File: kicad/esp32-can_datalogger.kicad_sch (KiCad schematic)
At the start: 60 parts, among them J1 USB_C_Receptacle_USB2.0_16P, J2 USB_C_Receptacle_USB2.0_16P, J3 USB_C_Receptacle_USB2.0_16P, J4 USB_C_Receptacle_USB2.0_16P, J5 USB_C_Receptacle_USB2.0_16P, J6 USB_C_Receptacle_USB2.0_16P, J7 Conn_Coaxial, J8 MicroSD, J9 Conn_01x04_Socket, SW1 SW_Push, SW2 SW_Push, SW3 SW_Push, SW4 SW_Push, U2 PA1616D, U3 PI4ULS3V204LEX, U4 AZ1117-1.8, U5 TJA1051T, U6 TJA1051T, U7 ICM-20948

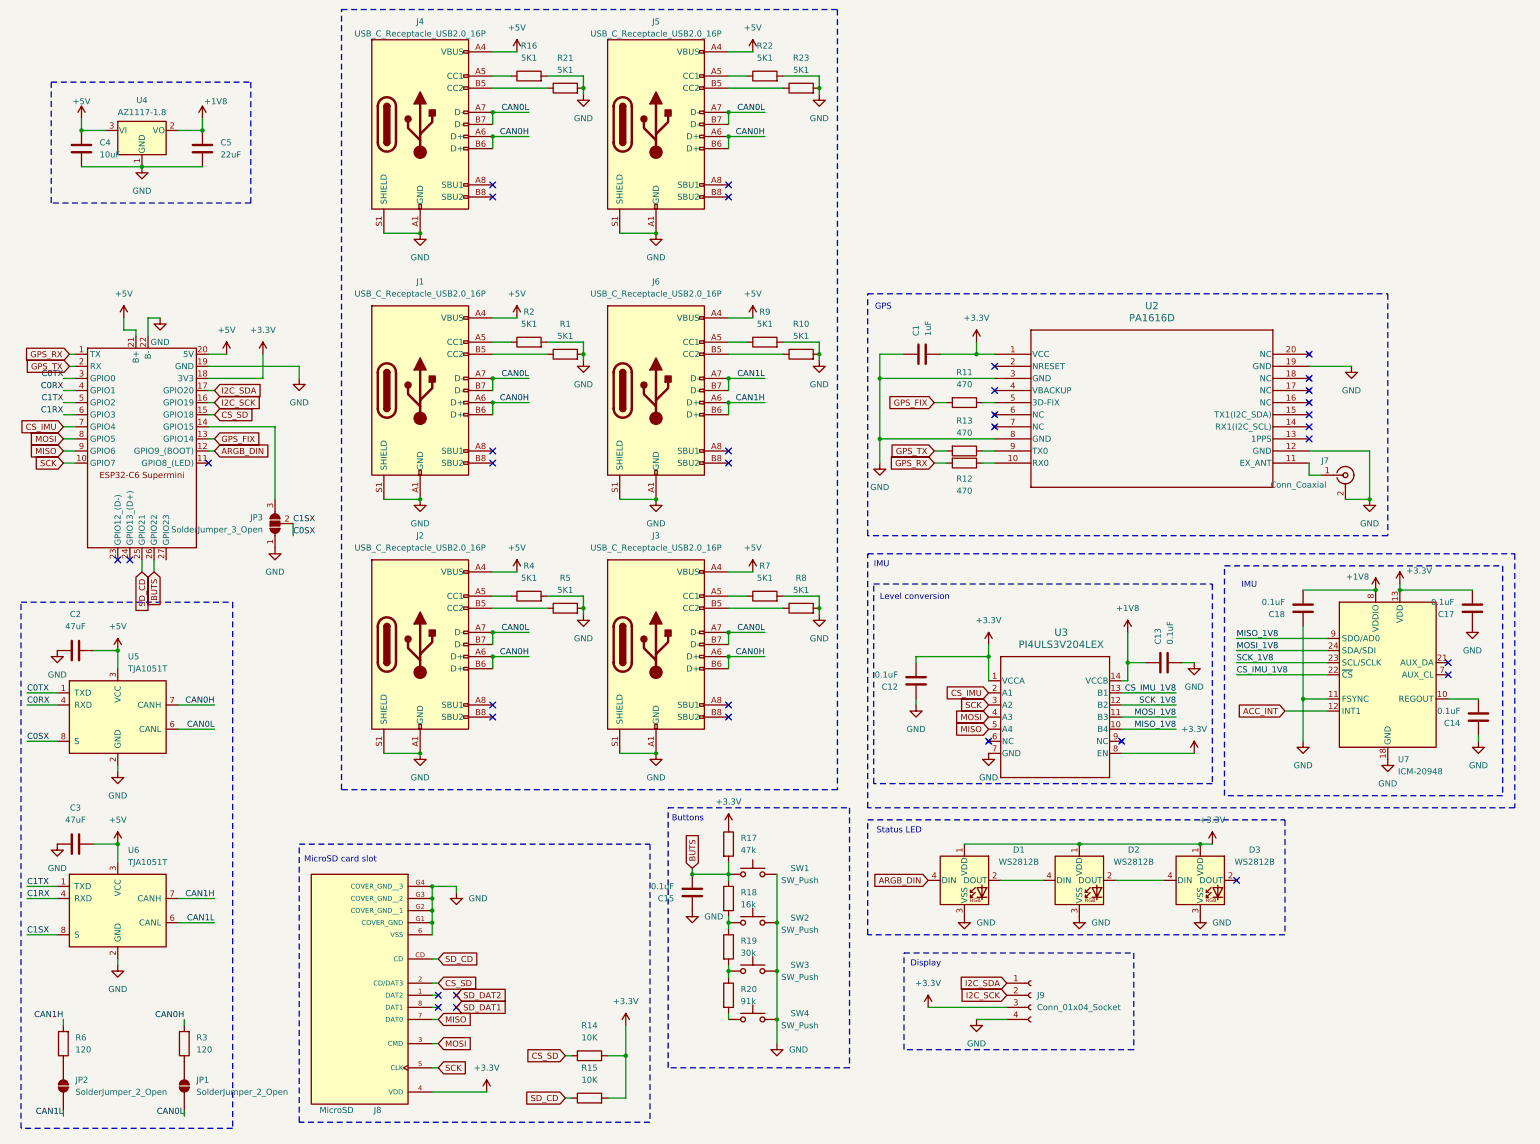
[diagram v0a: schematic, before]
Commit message: make pcb smaller
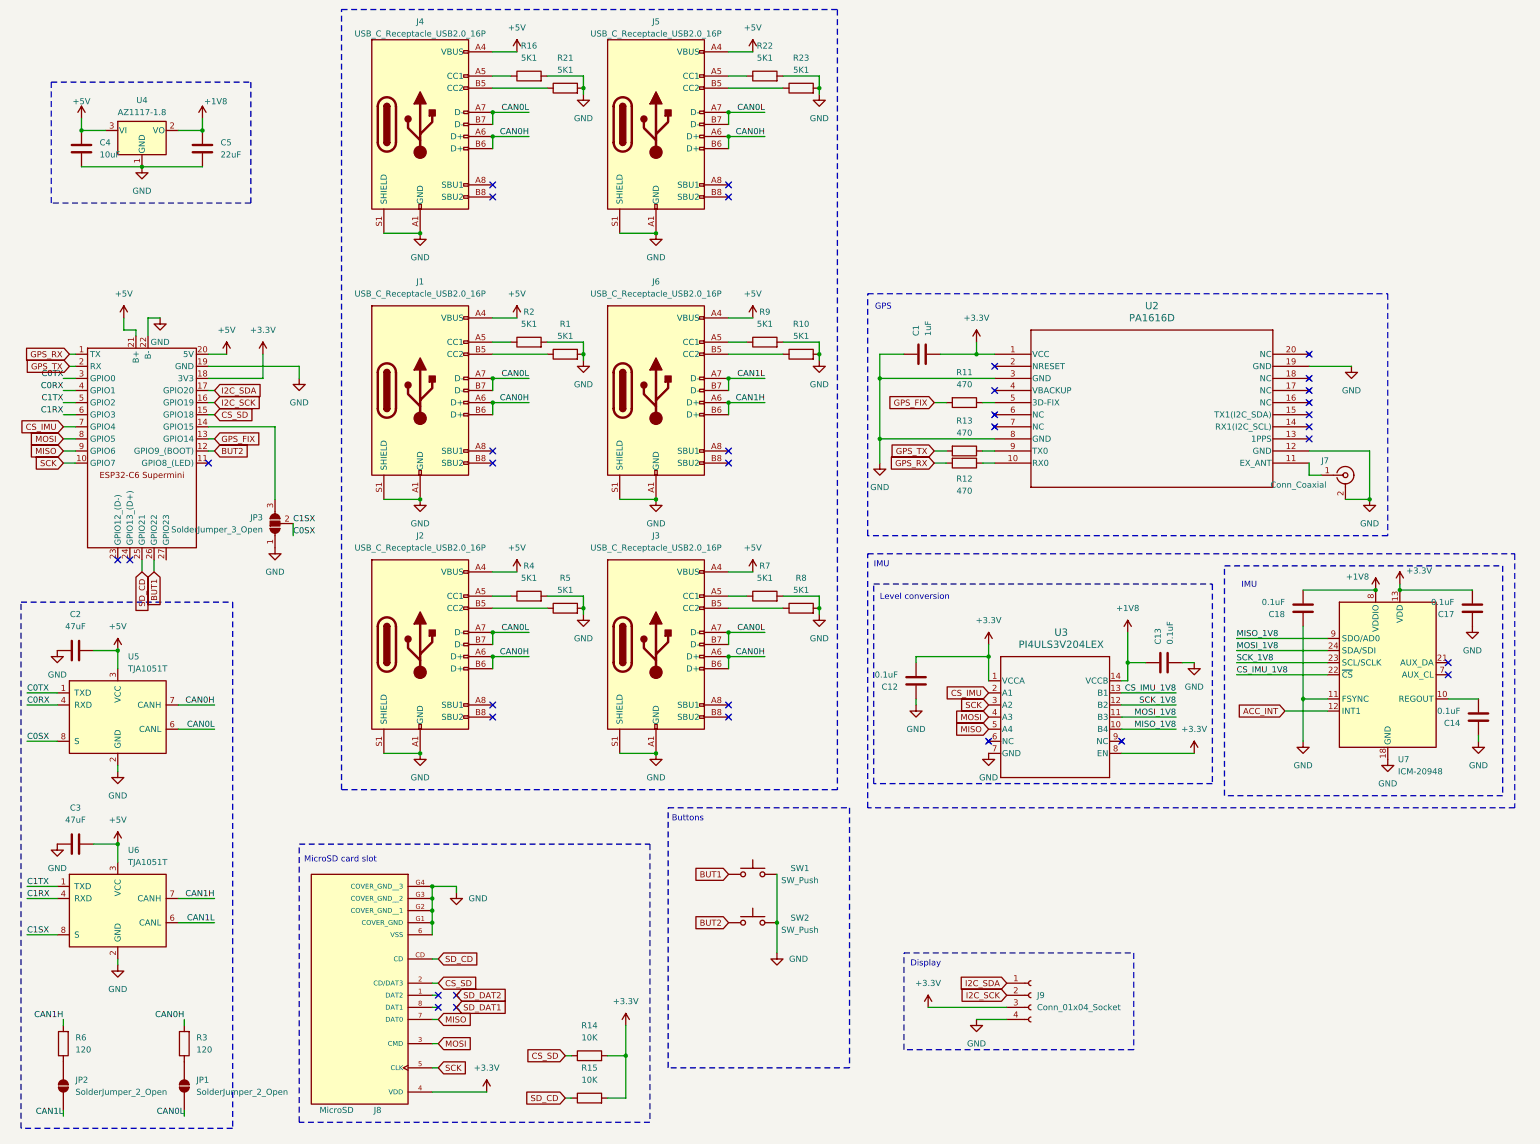
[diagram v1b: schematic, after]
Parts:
- removed C15: 0.1uF, Capacitor_SMD:C_1206_3216Metric, symbol Device:C
- removed D1, D2, D3: WS2812B, LED_SMD:LED_WS2812B_PLCC4_5.0x5.0mm_P3.2mm, symbol LED:WS2812B
- removed R17: 47k, Resistor_SMD:R_1206_3216Metric, symbol Device:R
- removed R18: 16k, Resistor_SMD:R_1206_3216Metric, symbol Device:R
- removed R19: 30k, Resistor_SMD:R_1206_3216Metric, symbol Device:R
- removed R20: 91k, Resistor_SMD:R_1206_3216Metric, symbol Device:R
- removed SW3, SW4: SW_Push, Button_Switch_SMD:SW_Push_SPST_NO_Alps_SKRK, symbol Switch:SW_Push
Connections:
- net ARGB_DIN is gone; now on net BUT2: U1.12 (GPIO9_(BOOT))
- net BUT2: now reaches SW2.1
- net BUTS renamed BUT1
- no-connect marks 35 -> 34
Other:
- note removed: "Status LED"

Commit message: make smaller still
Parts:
- removed J4, J5: USB_C_Receptacle_USB2.0_16P, Connector_USB:USB_C_Receptacle_GCT_USB4110, symbol Connector:USB_C_Receptacle_USB2.0_16P
- removed JP2: SolderJumper_2_Open, Jumper:SolderJumper-2_P1.3mm_Open_TrianglePad1.0x1.5mm, symbol Jumper:SolderJumper_2_Open
- removed JP3: SolderJumper_3_Open, Jumper:SolderJumper-3_P2.0mm_Open_TrianglePad1.0x1.5mm, symbol Jumper:SolderJumper_3_Open
- removed R16, R21, R22, R23: 5K1, Resistor_SMD:R_1206_3216Metric_Pad1.30x1.75mm_HandSolder, symbol Device:R
- removed R6: 120, Resistor_SMD:R_1206_3216Metric_Pad1.30x1.75mm_HandSolder, symbol Device:R
- J7: footprint Connector_Coaxial:U.FL_Hirose_U.FL-R-SMT-1_Vertical -> Connector_Coaxial:SMA_BAT_Wireless_BWSMA-KWE-Z001
- R1, R10, R2, R3, R4, R5, R7, R8, R9: footprint Resistor_SMD:R_1206_3216Metric_Pad1.30x1.75mm_HandSolder -> Resistor_SMD:R_0402_1005Metric_Pad0.72x0.64mm_HandSolder
- R11, R12, R13, R14, R15: footprint Resistor_SMD:R_1206_3216Metric -> Resistor_SMD:R_0402_1005Metric_Pad0.72x0.64mm_HandSolder
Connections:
- net C0SX: now also U1.14 (GPIO15)
- no-connect marks 34 -> 30

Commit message: layout refinement
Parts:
- added C15: 0.1uF, Capacitor_SMD:C_0402_1005Metric_Pad0.74x0.62mm_HandSolder, symbol Device:C
- C1, C12, C13, C14, C17, C18: footprint Capacitor_SMD:C_1206_3216Metric -> Capacitor_SMD:C_0402_1005Metric_Pad0.74x0.62mm_HandSolder
- C4, C5: footprint Capacitor_SMD:C_1206_3216Metric -> Capacitor_SMD:C_1206_3216Metric_Pad1.33x1.80mm_HandSolder
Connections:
- net +3.3V: now also C15.2
- net GND: now also C15.1

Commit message: update layout and schematic
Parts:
- added R16, R17: 10K, Resistor_SMD:R_0402_1005Metric_Pad0.72x0.64mm_HandSolder, symbol Device:R
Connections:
- net +3.3V: now also R16.2
- net BUT1: no longer SW1.1
- net C0RX: now also U1.8 (GPIO5); no longer U1.4 (GPIO1)
- net C0TX: now also U1.9 (GPIO6); no longer U1.3 (GPIO0)
- net C1TX: now also U1.7 (GPIO4); no longer U1.5 (GPIO2)
- net CS_IMU: now also U1.15 (GPIO18); no longer U1.7 (GPIO4)
- net CS_SD: now also U1.14 (GPIO15); no longer U1.15 (GPIO18)
- net GND: now also U5.8 (S), U6.8 (S), R17.1; no longer SW1.2
- net MISO: now also U1.4 (GPIO1); no longer U1.9 (GPIO6)
- net MOSI: now also U1.3 (GPIO0); no longer U1.8 (GPIO5)
- net SCK: now also U1.5 (GPIO2); no longer U1.10 (GPIO7)
- net BUT2: no longer names the net of U1.12 (GPIO9_(BOOT))
- net BUT2: no longer SW2.1
- removed net C0SX: U1.14 (GPIO15), U5.8 (S), U6.8 (S)
- new net: R17.2, SW1.2
- new net BUTS: R16.1, SW1.1, SW2.1, U1.10 (GPIO7)
- no-connect marks 30 -> 31
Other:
- note added: "Check if BUTS pin works Check if CS_SD and CS_IMU work Check if interrupt pin for IMU works"
- moved on the sheet: C4, C5, J9, SW1, SW2, U4

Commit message: complete layout - TODO check changes work
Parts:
- J1, J2, J3, J6: footprint Connector_USB:USB_C_Receptacle_GCT_USB4110 -> esp32-can_datalogger:USB_C_Receptacle_GCT_USB4110-grounded shield
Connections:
- net BUT1: no longer names the net of U1.26 (GPIO22)
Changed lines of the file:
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@@
 	(wire
 		(pts
-			(xy 41.91 73.66) (xy 41.91 76.2)
-		)
-		(stroke
-			(width 0)
-			(type default)
-		)
-	)
-	(wire
-		(pts
 			(xy 139.7 114.3) (xy 147.32 114.3)
 		)
@@
 		)
 	)
-	(global_label "BUT1"
-		(shape input)
-		(at 41.91 76.2 270)
-		(fields_autoplaced yes)
-		(effects
-			(font
-				(size 1.27 1.27)
-			)
-			(justify right)
-		)
-		(property "Intersheetrefs" "${INTERSHEET_REFS}"
-			(at 41.91 83.9628 90)
-			(hide yes)
-			(show_name no)
-			(do_not_autoplace no)
-			(effects
-				(font
-					(size 1.27 1.27)
-				)
-				(justify right)
-			)
-		)
-	)
 	(global_label "ACC_INT"
 		(shape input)
@@
 			)
 		)
-		(property "Footprint" "Connector_USB:USB_C_Receptacle_GCT_USB4110"
+		(property "Footprint" "esp32-can_datalogger:USB_C_Receptacle_GCT_USB4110-grounded shield"
 			(at 151.13 91.44 0)
 			(hide yes)
@@
 			)
 		)
-		(property "Footprint" "Connector_USB:USB_C_Receptacle_GCT_USB4110"
+		(property "Footprint" "esp32-can_datalogger:USB_C_Receptacle_GCT_USB4110-grounded shield"
 			(at 151.13 38.1 0)
 			(hide yes)
@@
 			)
 		)
-		(property "Footprint" "Connector_USB:USB_C_Receptacle_GCT_USB4110"
+		(property "Footprint" "esp32-can_datalogger:USB_C_Receptacle_GCT_USB4110-grounded shield"
 			(at 101.6 91.44 0)
 			(hide yes)
@@
 			)
 		)
-		(property "Footprint" "Connector_USB:USB_C_Receptacle_GCT_USB4110"
+		(property "Footprint" "esp32-can_datalogger:USB_C_Receptacle_GCT_USB4110-grounded shield"
 			(at 101.6 38.1 0)
 			(hide yes)

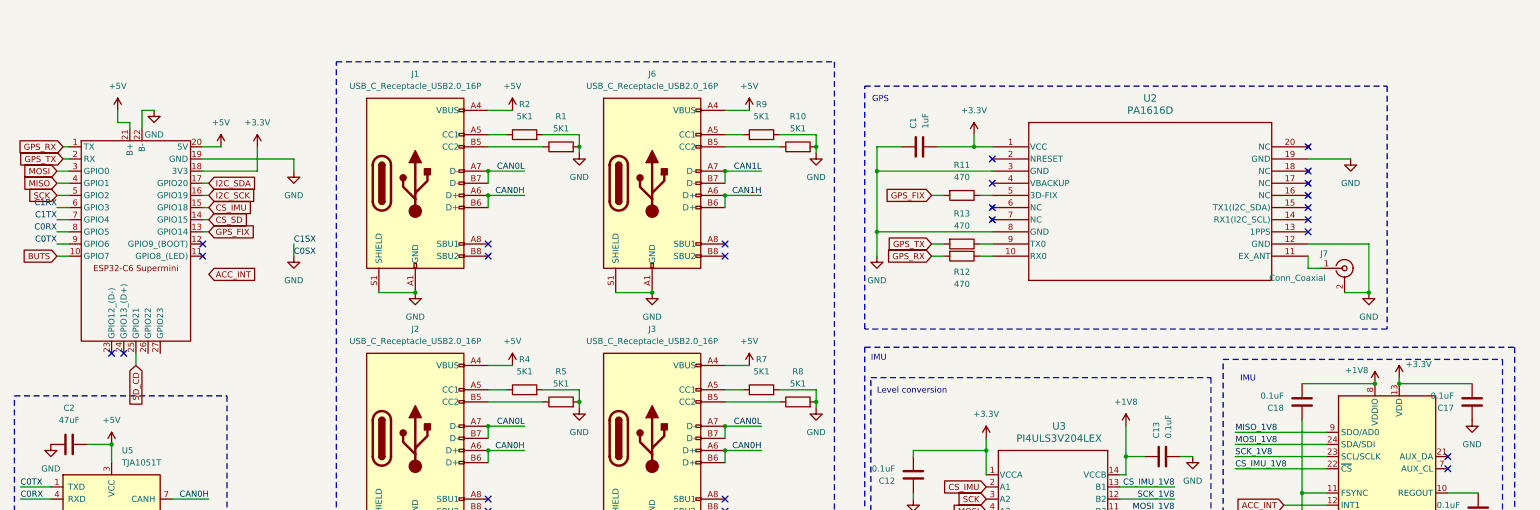
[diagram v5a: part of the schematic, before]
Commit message: add vbackup 1220 cell
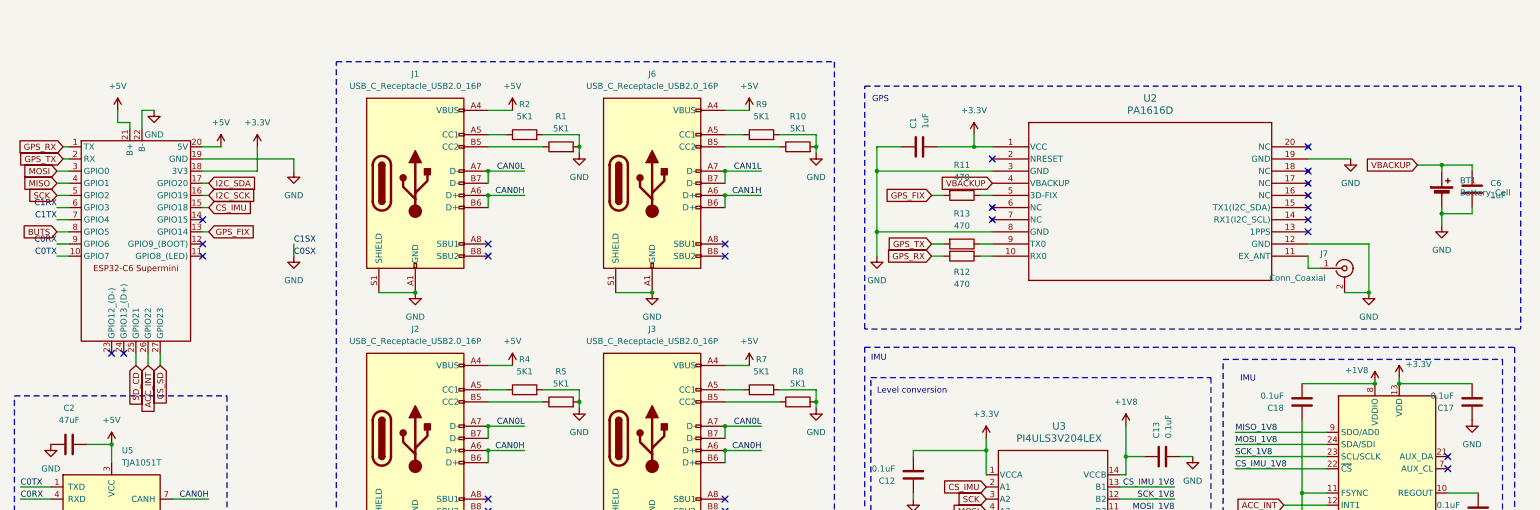
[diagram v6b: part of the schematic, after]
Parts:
- added BT1: Battery_Cell, esp32-can_datalogger:BAT_1056, symbol Device:Battery_Cell
- added C6: 1uF, Capacitor_SMD:C_0402_1005Metric_Pad0.74x0.62mm_HandSolder, symbol Device:C
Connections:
- net ACC_INT: now also U1.26 (GPIO22)
- net BUTS: now also U1.8 (GPIO5); no longer U1.10 (GPIO7)
- net C0RX: now also U1.9 (GPIO6); no longer U1.8 (GPIO5)
- net C0TX: now also U1.10 (GPIO7); no longer U1.9 (GPIO6)
- net CS_SD: now also U1.27 (GPIO23); no longer U1.14 (GPIO15)
- net GND: now also BT1.2 (-), C6.2
- net VBACKUP: now reaches U2.4 (VBACKUP)
- net VBACKUP: now also BT1.1 (+), C6.1
